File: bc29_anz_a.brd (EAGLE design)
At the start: 100 x 80 mm, 10 parts, among them IC2 MM74C945N, J1 2520-5

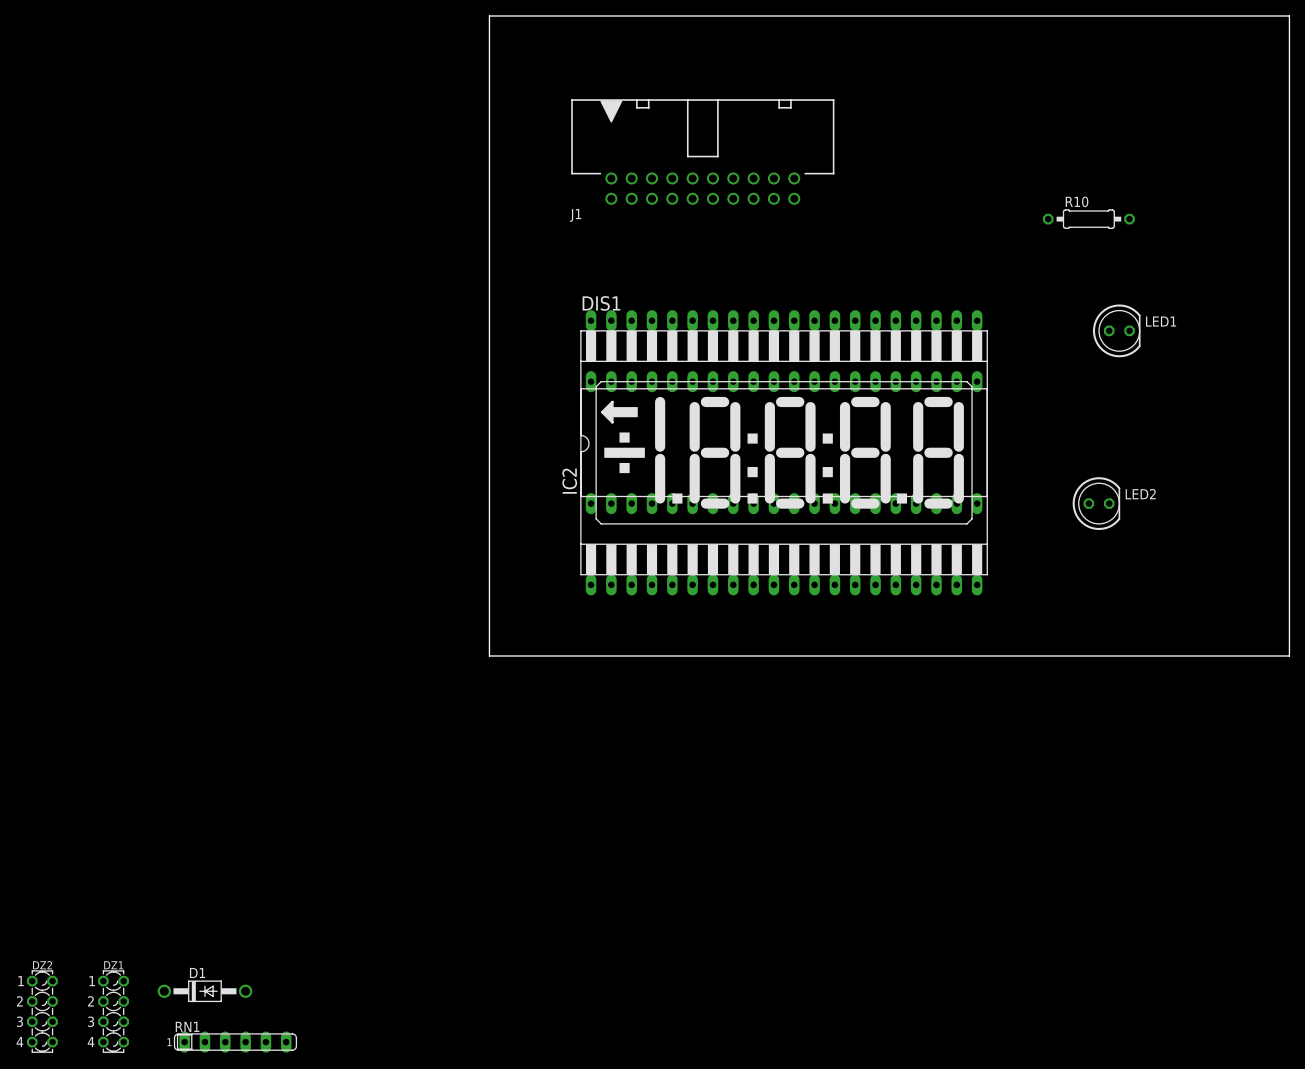
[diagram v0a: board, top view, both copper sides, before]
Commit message: Incorperate display module knowldge
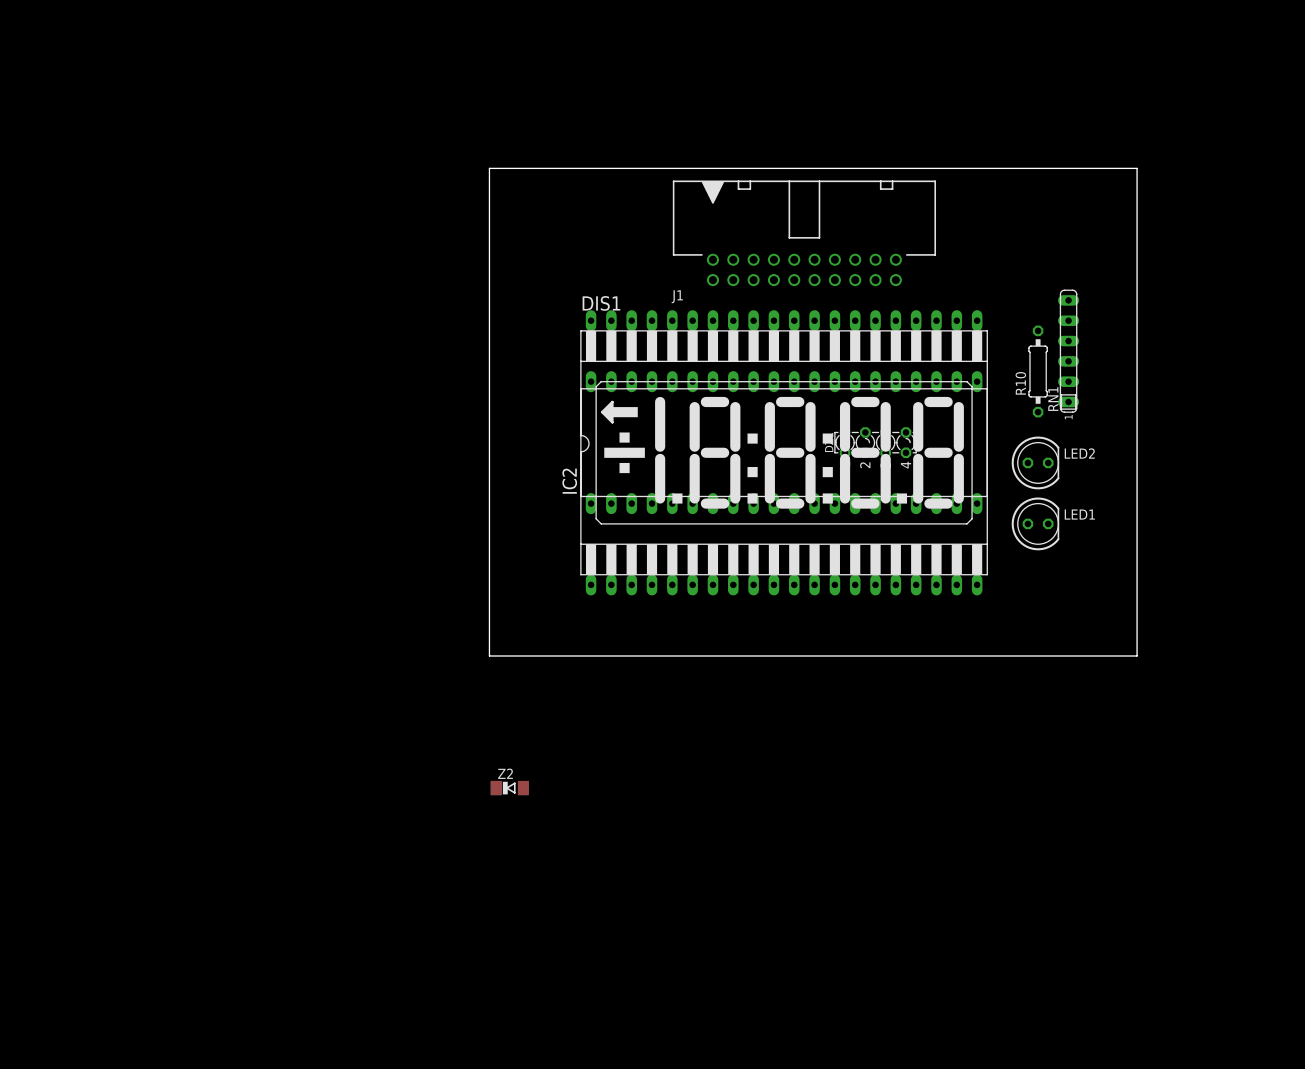
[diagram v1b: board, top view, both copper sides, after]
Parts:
- removed D1: 1N4004, diode:DO41-10
- removed DZ2: LZR184, led:LZR184
- added Z2: 12.1V, diode:SOD80C
- moved RN1 135.3 mm to (72.4, 38.1), turned to 90 degrees
- moved DZ1 118.9 mm to (48.3, 26.7), turned to 90 degrees
- moved LED1 26.2 mm to (68.6, 16.5)
- moved R10 20.1 mm to (68.6, 35.6), turned to 90 degrees
- moved J1 16.3 mm to (39.4, 48.3)
- moved LED2 9.16 mm to (68.6, 24.1)
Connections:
- net !CARRY renamed !LCD_COUNTER_CARRY
- net !DOWN renamed LCD_COUNTER_UP
- net !LCD_RESET renamed !LCD_COUNTER_RESET
- net BLANK renamed LCD_COUNTER_BLANK
- net ENABLE renamed LCD_COUNTER_ENABLE
- removed net LCD_45_HZ: IC2.5, J1.19
- new net !LCD_COUNTER_BACKPLANE: DIS1.1, DIS1.40, IC2.5, J1.19
- new net !LCD_COUNTER_CLK: J1.15
- new net N$1: R10.1, RN1.1, Z2.C
- new net N$2: DZ1.A4, RN1.6
- new net N$3: DZ1.A3, RN1.5
- new net N$4: DZ1.A2, RN1.4
- new net N$5: DZ1.A1, RN1.3
- net !UP_DOWN_CLK: no longer J1.15
- net 12+: now also R10.2
- net 12-: now also DZ1.K1, DZ1.K2, DZ1.K3, DZ1.K4, Z2.A
- net LCD_COLON: now also DIS1.28
- net LCD_DECIMAL_POINT: now also DIS1.12
- net LCD_MINUS_SIGN: now also DIS1.2
- net LCD_ONE_MSD: now also DIS1.3
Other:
- board size 100 x 80 mm -> 81 x 61 mm

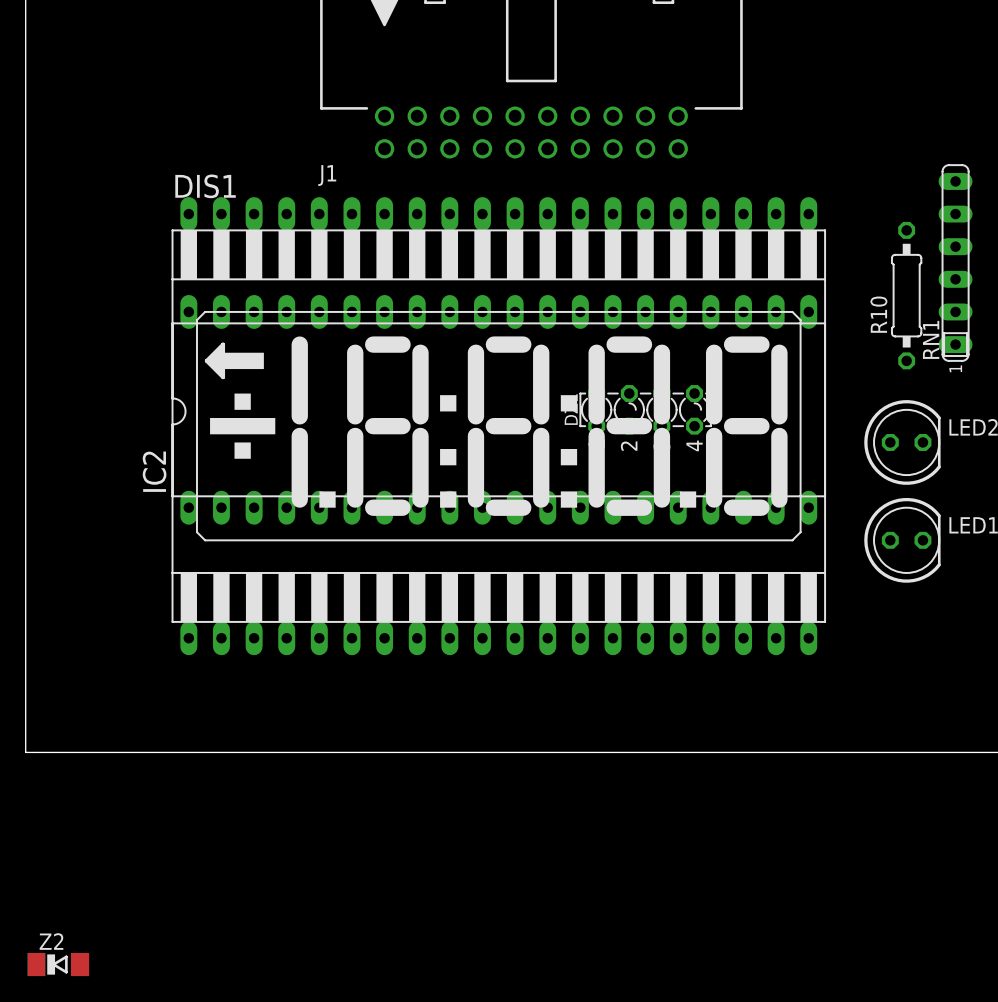
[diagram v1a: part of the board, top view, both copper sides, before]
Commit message: Clean up net names
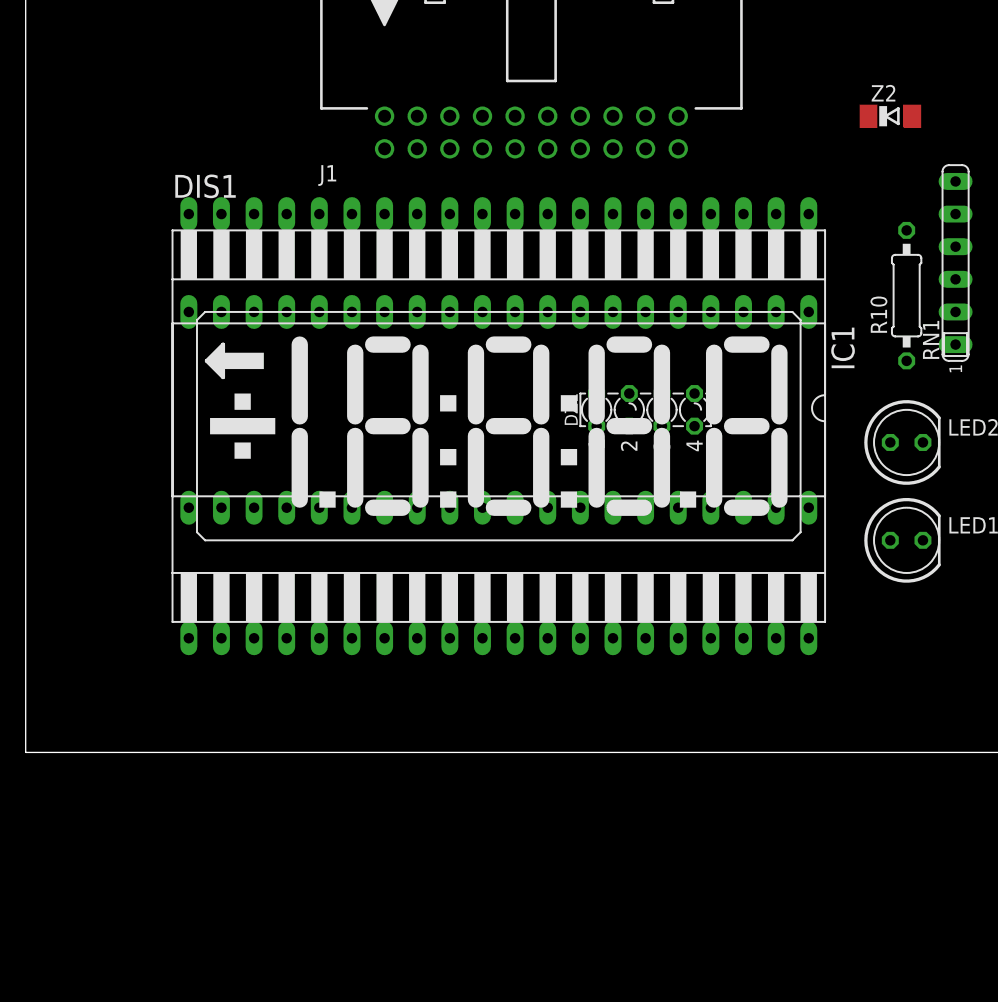
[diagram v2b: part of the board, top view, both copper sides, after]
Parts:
- IC1: value MM74C945N -> MM74C945
- moved Z2 92.5 mm to (67.3, 49.5)
- turned IC1 to 180 degrees
- renumbered IC2 to IC1
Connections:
- net !LCD_COUNTER_BACKPLANE renamed LCD_COUNTER_BACKPLANE
- net N$1 renamed LED_V+
- net N$2 renamed BL3
- net N$3 renamed BL2
- net N$4 renamed BL1
- net N$5 renamed BL0
- removed net !LCD_COUNTER_CLK: J1.15
- removed net !UP_DOWN_CLK: IC1.32
- removed net OSC-GND: IC1.36
- new net A1: DIS1.21, IC1.37
- new net A2: DIS1.25, IC1.6
- new net A3: DIS1.30, IC1.13
- new net A4: DIS1.35, IC1.20
- new net B1: DIS1.20, IC1.38
- new net B2: DIS1.24, IC1.7
- new net B3: DIS1.29, IC1.14
- new net B4: DIS1.34, IC1.21
- new net C1: DIS1.19, IC1.39
- new net C2: DIS1.15, IC1.8
- new net C3: DIS1.11, IC1.15
- new net C4: DIS1.7, IC1.22
- new net D1: DIS1.18, IC1.40
- new net D2: DIS1.14, IC1.9
- new net D3: DIS1.10, IC1.16
- new net D4: DIS1.6, IC1.23
- new net E1: DIS1.17, IC1.2
- new net E2: DIS1.13, IC1.10
- new net E3: DIS1.9, IC1.17
- new net E4: DIS1.5, IC1.24
- new net F1: DIS1.22, IC1.4
- new net F2: DIS1.26, IC1.12
- new net F3: DIS1.31, IC1.19
- new net F4: DIS1.36, IC1.26
- new net G1: DIS1.23, IC1.3
- new net G2: DIS1.27, IC1.11
- new net G3: DIS1.32, IC1.18
- new net G4: DIS1.37, IC1.25
- new net LCD_COUNTER_CLK: IC1.32, J1.15
